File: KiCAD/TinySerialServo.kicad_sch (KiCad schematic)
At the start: 24 parts, among them J1 Conn_01x03_Pin, J2 Conn_01x04_Pin, Q1 NPN, SW1 SW_Push, SW2 SW_Push, U1 PIC12LF1840-xSN

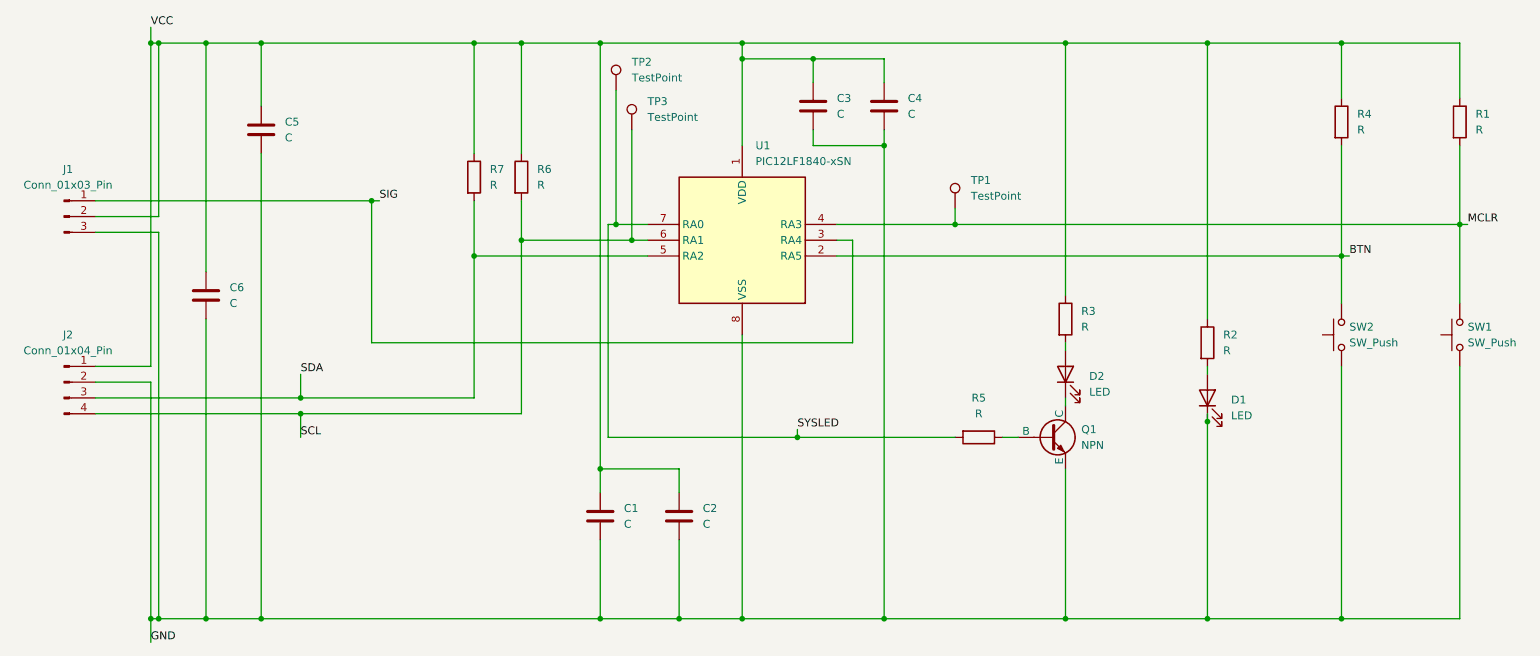
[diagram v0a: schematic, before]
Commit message: Removed the NPN; Rerouted traces; Remapped pinouts; Changed board dimentions; Added graphics to board
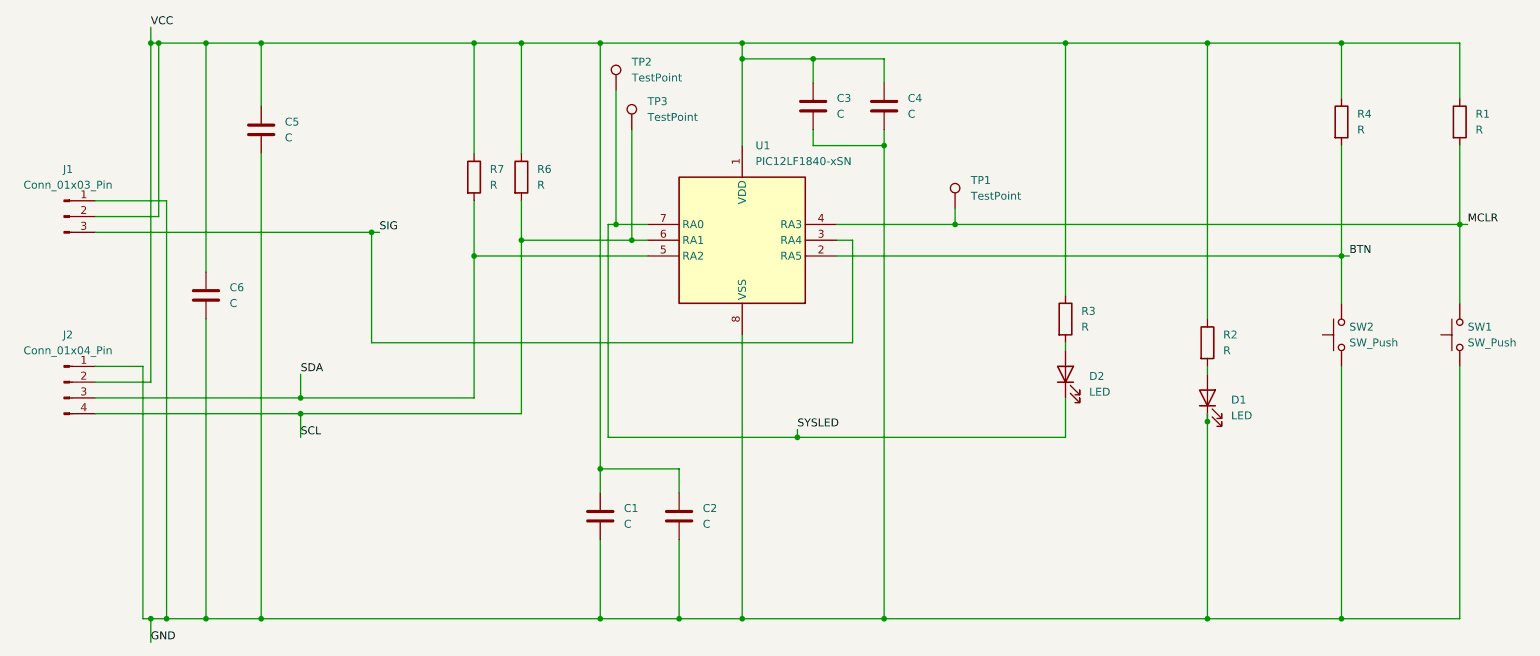
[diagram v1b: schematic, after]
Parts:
- removed Q1: NPN, Package_TO_SOT_SMD:SOT-23-3, symbol Simulation_SPICE:NPN
- removed R5: R, Resistor_SMD:R_0805_2012Metric_Pad1.20x1.40mm_HandSolder, symbol Device:R
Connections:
- net GND: now also J1.1 (Pin_1), J2.1 (Pin_1); no longer J1.3 (Pin_3), J2.2 (Pin_2)
- net SIG: now also J1.3 (Pin_3); no longer J1.1 (Pin_1)
- net SYSLED: now also D2.1 (K)
- net VCC: now also J2.2 (Pin_2); no longer J2.1 (Pin_1)

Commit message: PCB Sent to OSH PARK
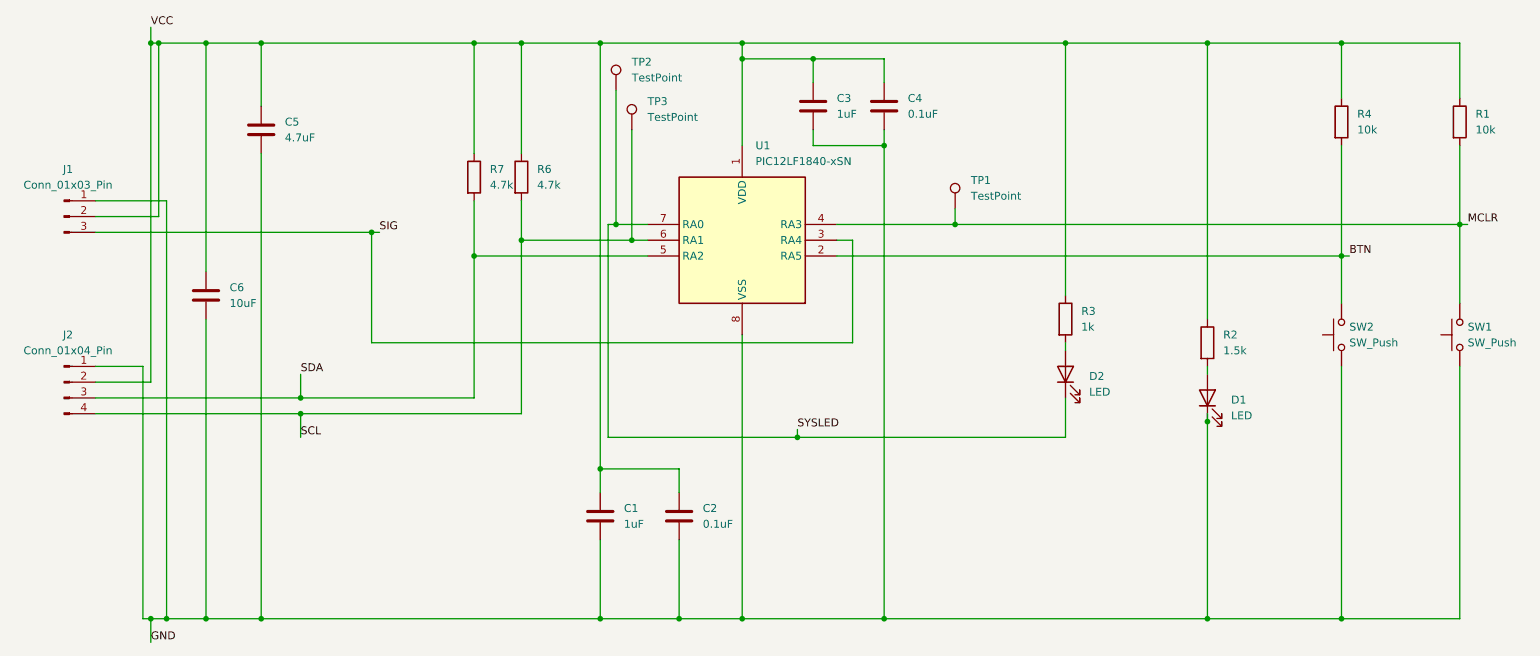
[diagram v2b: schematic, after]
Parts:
- C1, C3: value C -> 1uF
- C2, C4: value C -> 0.1uF
- C5: value C -> 4.7uF
- C6: value C -> 10uF
- R1, R4: value R -> 10k
- R2: value R -> 1.5k
- R3: value R -> 1k
- R6, R7: value R -> 4.7k
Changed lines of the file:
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@@
 			)
 		)
-		(property "Value" "R"
+		(property "Value" "10k"
 			(at 240.03 67.3099 0)
 			(effects
@@
 			)
 		)
-		(property "Value" "C"
+		(property "Value" "1uF"
 			(at 156.21 64.7699 0)
 			(effects
@@
 			)
 		)
-		(property "Value" "R"
+		(property "Value" "1.5k"
 			(at 218.44 102.8699 0)
 			(effects
@@
 			)
 		)
-		(property "Value" "R"
+		(property "Value" "1k"
 			(at 195.58 99.0599 0)
 			(effects
@@
 			)
 		)
-		(property "Value" "R"
+		(property "Value" "10k"
 			(at 259.08 67.3099 0)
 			(effects
@@
 			)
 		)
-		(property "Value" "C"
+		(property "Value" "4.7uF"
 			(at 67.31 68.5799 0)
 			(effects
@@
 			)
 		)
-		(property "Value" "R"
+		(property "Value" "4.7k"
 			(at 100.33 76.1999 0)
 			(effects
@@
 			)
 		)
-		(property "Value" "C"
+		(property "Value" "1uF"
 			(at 121.92 130.8099 0)
 			(effects
@@
 			)
 		)
-		(property "Value" "C"
+		(property "Value" "0.1uF"
 			(at 167.64 64.7699 0)
 			(effects
@@
 			)
 		)
-		(property "Value" "R"
+		(property "Value" "4.7k"
 			(at 107.95 76.1999 0)
 			(effects
@@
 			)
 		)
-		(property "Value" "C"
+		(property "Value" "0.1uF"
 			(at 134.62 130.8099 0)
 			(effects
@@
 			)
 		)
-		(property "Value" "C"
+		(property "Value" "10uF"
 			(at 58.42 95.2499 0)
 			(effects
